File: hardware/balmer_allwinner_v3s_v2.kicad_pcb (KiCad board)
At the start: 4 copper layers, 60 x 60 mm, 119 parts, among them J1 JAE_SIM_Card_SF72S006, J11 Micro_SD_Card_Ebay, J2 UART, J3 Bus_PCI_Express_Mini, J4 USB_C_Receptacle, J8 HR911105_RJ45, SW2 SW_MEC_5G, U1 AllwinnerV3S, U10 TLV62568DBV, U2 CH340C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

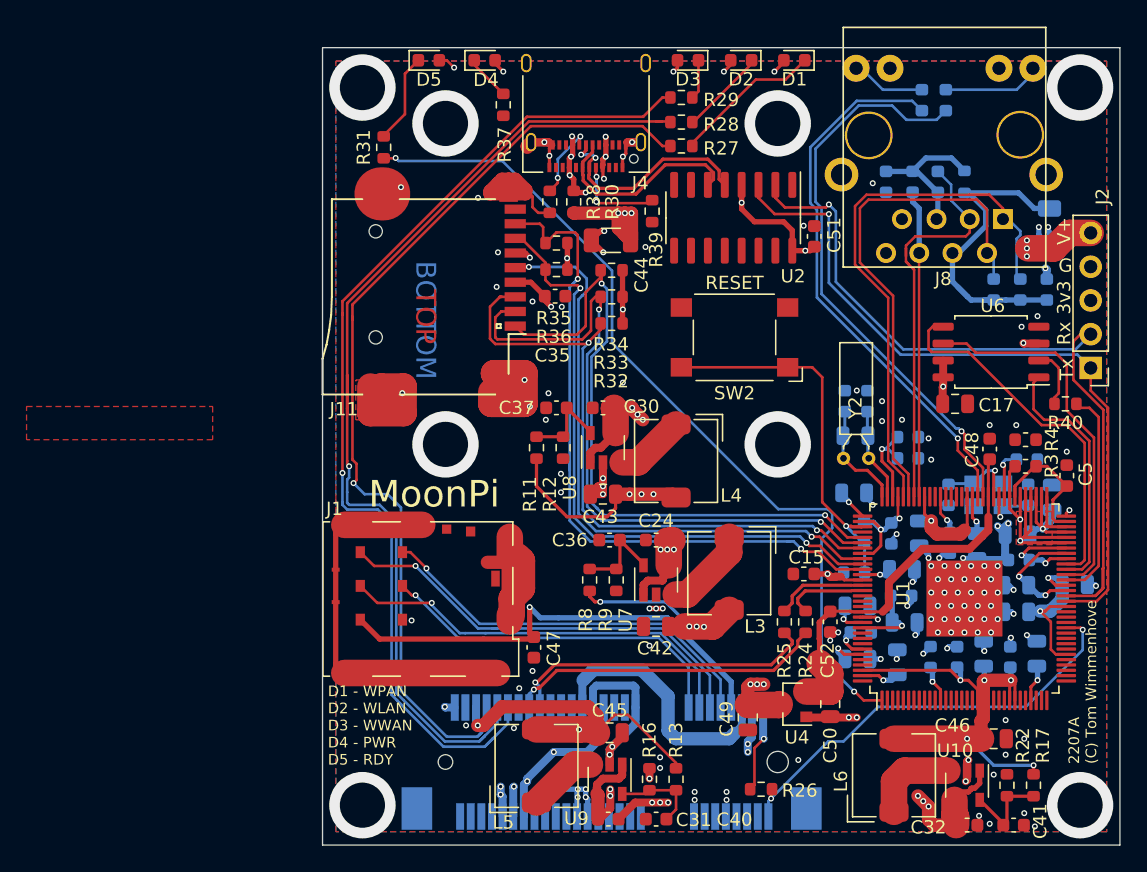
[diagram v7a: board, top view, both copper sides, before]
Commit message: Changed mPCIe mounting holes for PCB inserts: https://www.farnell.com/cad/2720308.pdf (length may vary
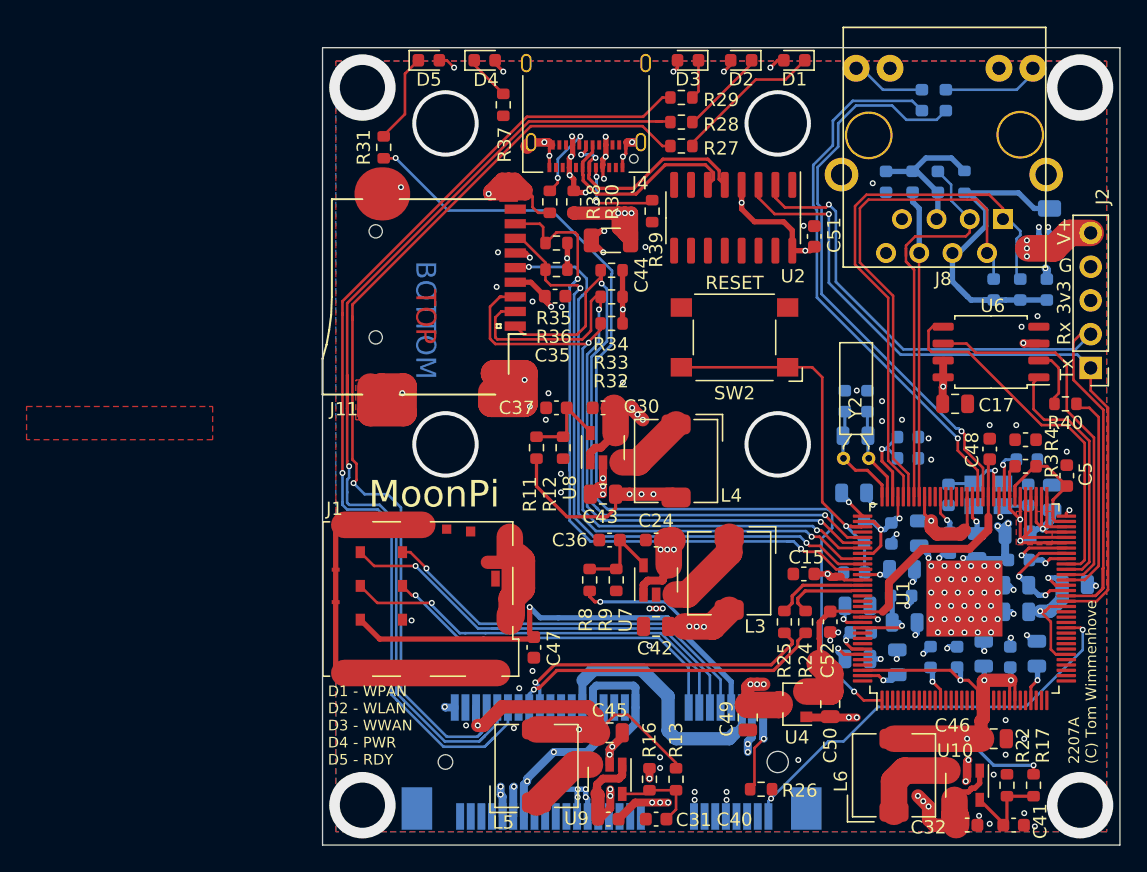
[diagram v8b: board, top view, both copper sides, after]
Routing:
- net SDC1_D2: track 65.1 -> 73.7 mm
